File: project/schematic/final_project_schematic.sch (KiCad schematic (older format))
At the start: 5 parts

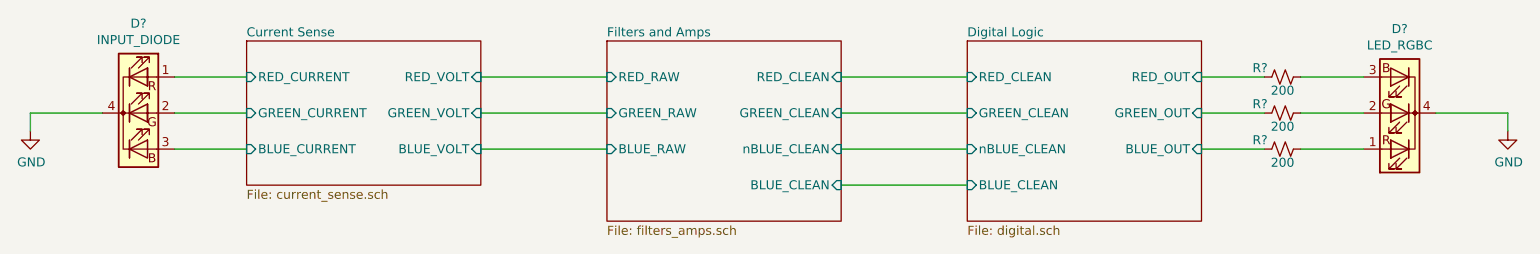
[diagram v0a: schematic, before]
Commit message: switch to high pass filters
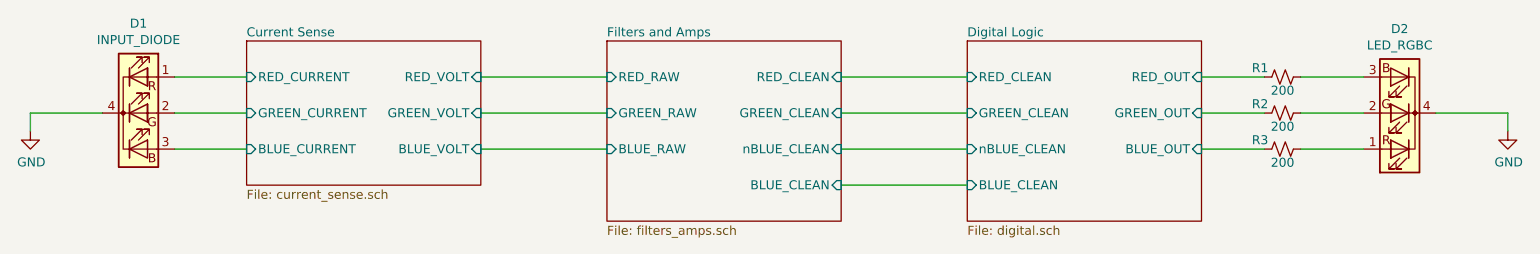
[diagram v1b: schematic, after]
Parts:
- gave numbers to parts that had none: 5
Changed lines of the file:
@@
 EESchema Schematic File Version 4
+LIBS:final_project_schematic-cache
 EELAYER 30 0
 EELAYER END
@@
 $EndDescr
 $Comp
-L Device:LED_RGBC D?
+L Device:LED_RGBC D1
 U 1 1 5DEDB632
 P 1900 4050
-F 0 "D?" H 1900 4547 50  0000 C CNN
+F 0 "D1" H 1900 4547 50  0000 C CNN
 F 1 "INPUT_DIODE" H 1900 4456 50  0000 C CNN
 F 2 "" H 1900 4000 50  0001 C CNN
@@
 $EndComp
 $Comp
-L power:GND #PWR?
+L power:GND #PWR01
 U 1 1 5DEDE851
 P 1300 4150
-F 0 "#PWR?" H 1300 3900 50  0001 C CNN
+F 0 "#PWR01" H 1300 3900 50  0001 C CNN
 F 1 "GND" H 1305 3977 50  0000 C CNN
 F 2 "" H 1300 4150 50  0001 C CNN
@@
 	9500 4150 9500 4050
 $Comp
-L power:GND #PWR?
+L power:GND #PWR02
 U 1 1 5E3BAB6B
 P 9500 4150
-F 0 "#PWR?" H 9500 3900 50  0001 C CNN
+F 0 "#PWR02" H 9500 3900 50  0001 C CNN
 F 1 "GND" H 9505 3977 50  0000 C CNN
 F 2 "" H 9500 4150 50  0001 C CNN
@@
 	8350 4250 8700 4250
 $Comp
-L Device:R_Small_US R?
+L Device:R_Small_US R3
 U 1 1 5E3B9BAB
 P 8250 4250
-F 0 "R?" V 8200 4125 50  0000 C CNN
+F 0 "R3" V 8200 4125 50  0000 C CNN
 F 1 "200" V 8325 4250 50  0000 C CNN
 F 2 "" H 8250 4250 50  0001 C CNN
@@
 	8350 4050 8700 4050
 $Comp
-L Device:R_Small_US R?
+L Device:R_Small_US R2
 U 1 1 5E3B95D0
 P 8250 4050
-F 0 "R?" V 8200 3925 50  0000 C CNN
+F 0 "R2" V 8200 3925 50  0000 C CNN
 F 1 "200" V 8325 4050 50  0000 C CNN
 F 2 "" H 8250 4050 50  0001 C CNN
@@
 	8350 3850 8700 3850
 $Comp
-L Device:R_Small_US R?
+L Device:R_Small_US R1
 U 1 1 5E396A01
 P 8250 3850
-F 0 "R?" V 8200 3725 50  0000 C CNN
+F 0 "R1" V 8200 3725 50  0000 C CNN
 F 1 "200" V 8325 3850 50  0000 C CNN
 F 2 "" H 8250 3850 50  0001 C CNN
@@
 $EndComp
 $Comp
-L Device:LED_RGBC D?
+L Device:LED_RGBC D2
 U 1 1 5E2679CC
 P 8900 4050
-F 0 "D?" H 8900 3583 50  0000 C CNN
+F 0 "D2" H 8900 3583 50  0000 C CNN
 F 1 "LED_RGBC" H 8900 3674 50  0000 C CNN
 F 2 "" H 8900 4000 50  0001 C CNN
